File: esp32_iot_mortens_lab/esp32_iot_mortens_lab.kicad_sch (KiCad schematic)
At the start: 55 parts, among them J1 Conn_01x04, J2 Screw_Terminal_01x03, J3 Screw_Terminal_01x08, J4 Screw_Terminal_01x02, J5 USB_C_Receptacle_USB2.0_16P, K1 RT314A05, Q1 UMH3N, Q2 BC817, SW1 SW_SPST, U1 ESP32-WROOM-32D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

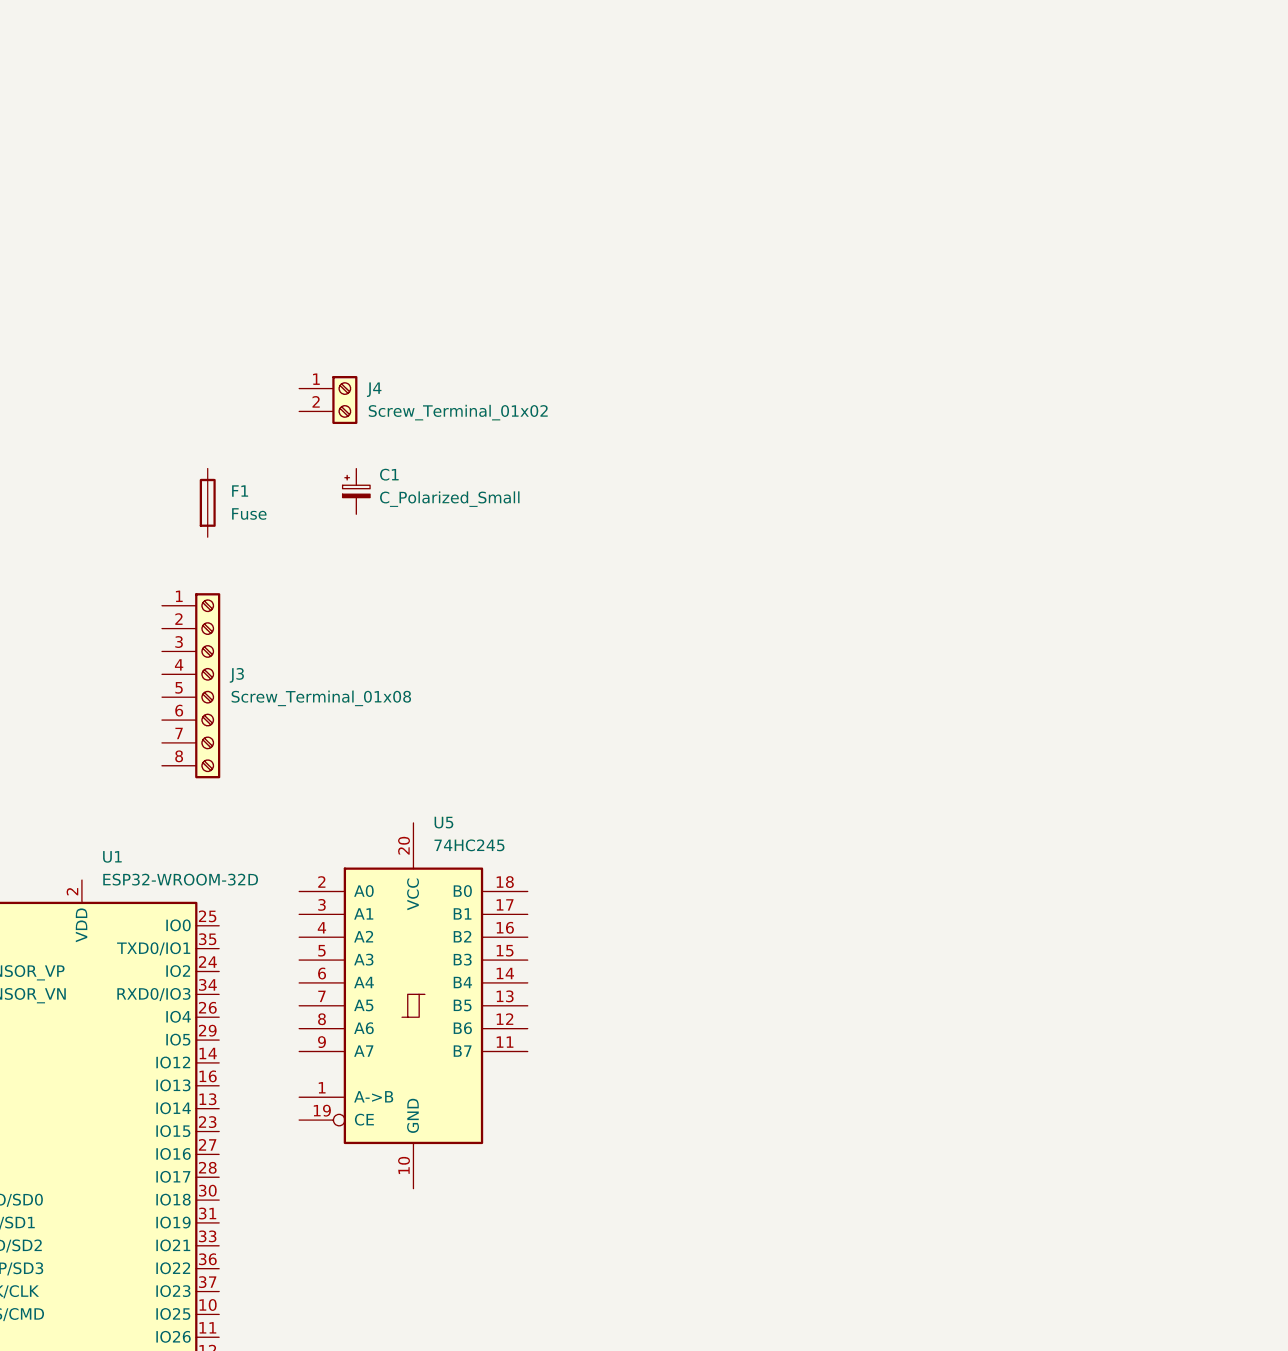
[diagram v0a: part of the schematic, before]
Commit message: bi-directional transceiver subcircuit
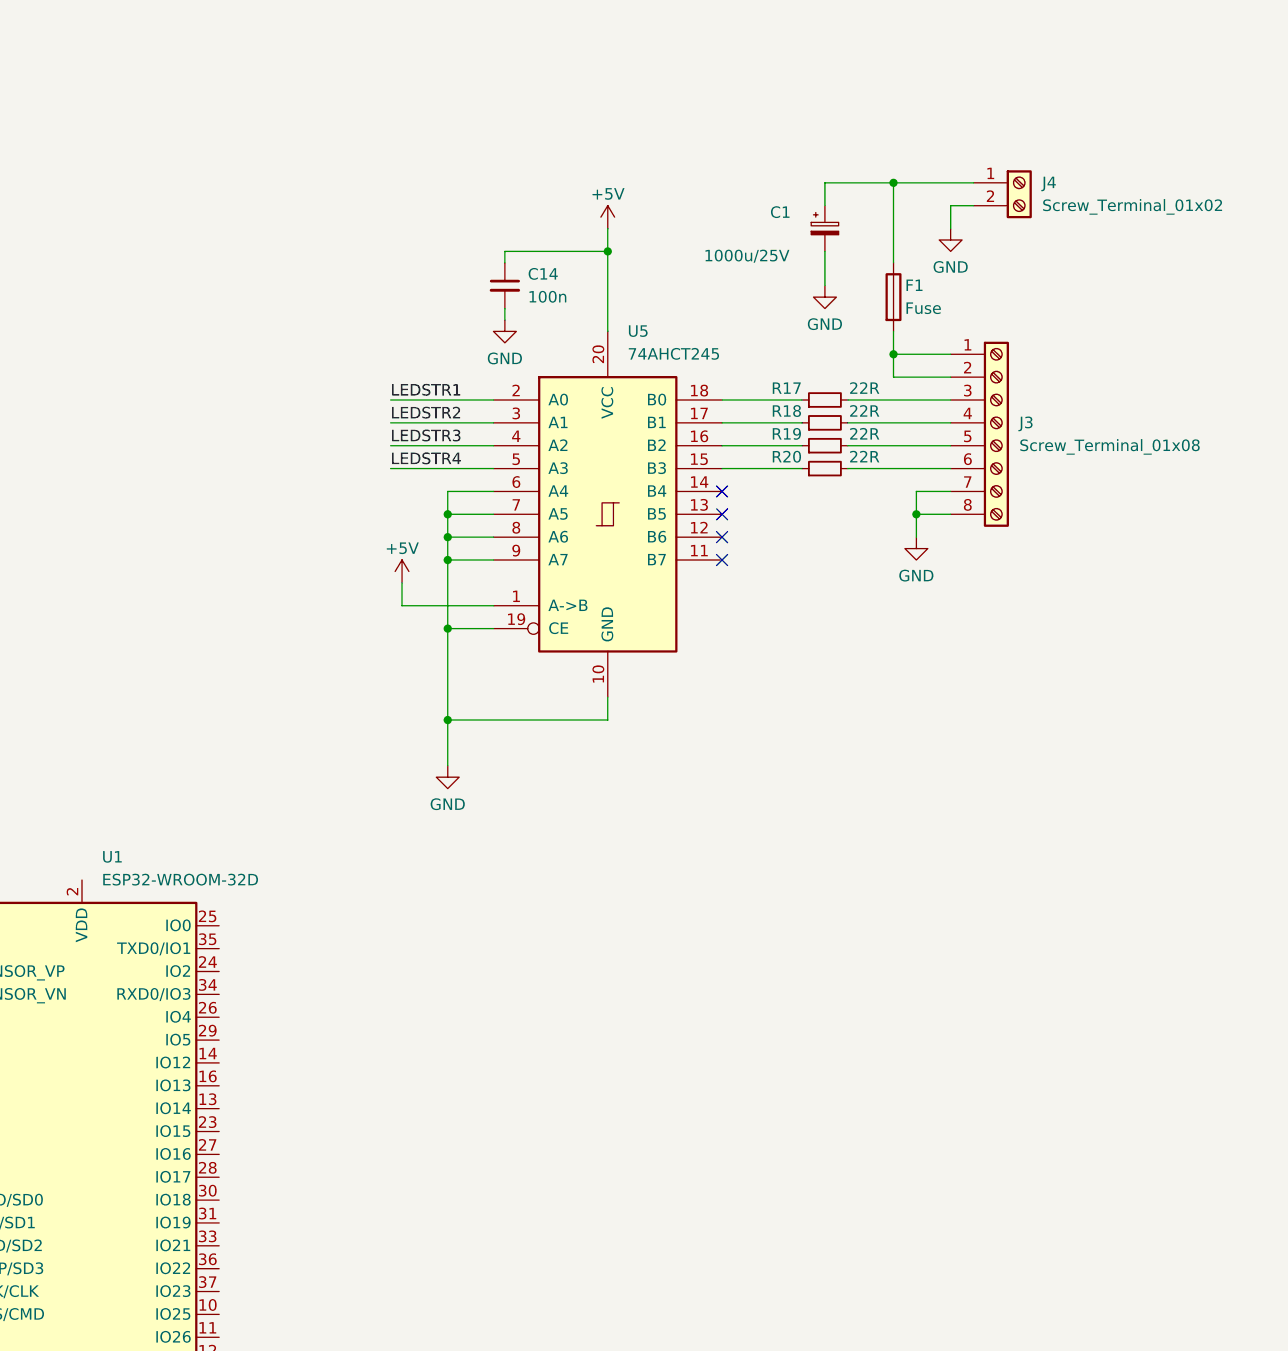
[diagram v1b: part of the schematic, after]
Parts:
- added C14: 100n, symbol Device:C_Small
- added R17, R18, R19, R20: 22R, symbol Device:R_Small
- C1: value C_Polarized_Small -> 1000u/25V
- U5: value 74HC245 -> 74AHCT245
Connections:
- net +3.3VA: now also U5.1 (A->B), U5.20 (VCC), C14.1
- net GND: now also C1.2, J3.7 (Pin_7), J3.8 (Pin_8), J4.2 (Pin_2), U5.10 (GND), U5.19 (CE), U5.6 (A4), U5.7 (A5), U5.8 (A6), U5.9 (A7), C14.2
- net at J4.1 (Pin_1): now also C1.1, F1.1
- net at J3.1 (Pin_1): now also F1.2, J3.2 (Pin_2)
- net at J3.3 (Pin_3): now also R17.2
- net at J3.4 (Pin_4): now also R18.2
- net at J3.5 (Pin_5): now also R19.2
- net at J3.6 (Pin_6): now also R20.2
- net at U5.15 (B3): now also R20.1
- net at U5.16 (B2): now also R19.1
- net at U5.17 (B1): now also R18.1
- net at U5.18 (B0): now also R17.1
- net LEDSTR1: now reaches U5.2 (A0)
- net LEDSTR2: now reaches U5.3 (A1)
- net LEDSTR3: now reaches U5.4 (A2)
- net LEDSTR4: now reaches U5.5 (A3)
- no-connect marks 0 -> 4
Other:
- moved on the sheet: C1, F1, J3, J4, U5

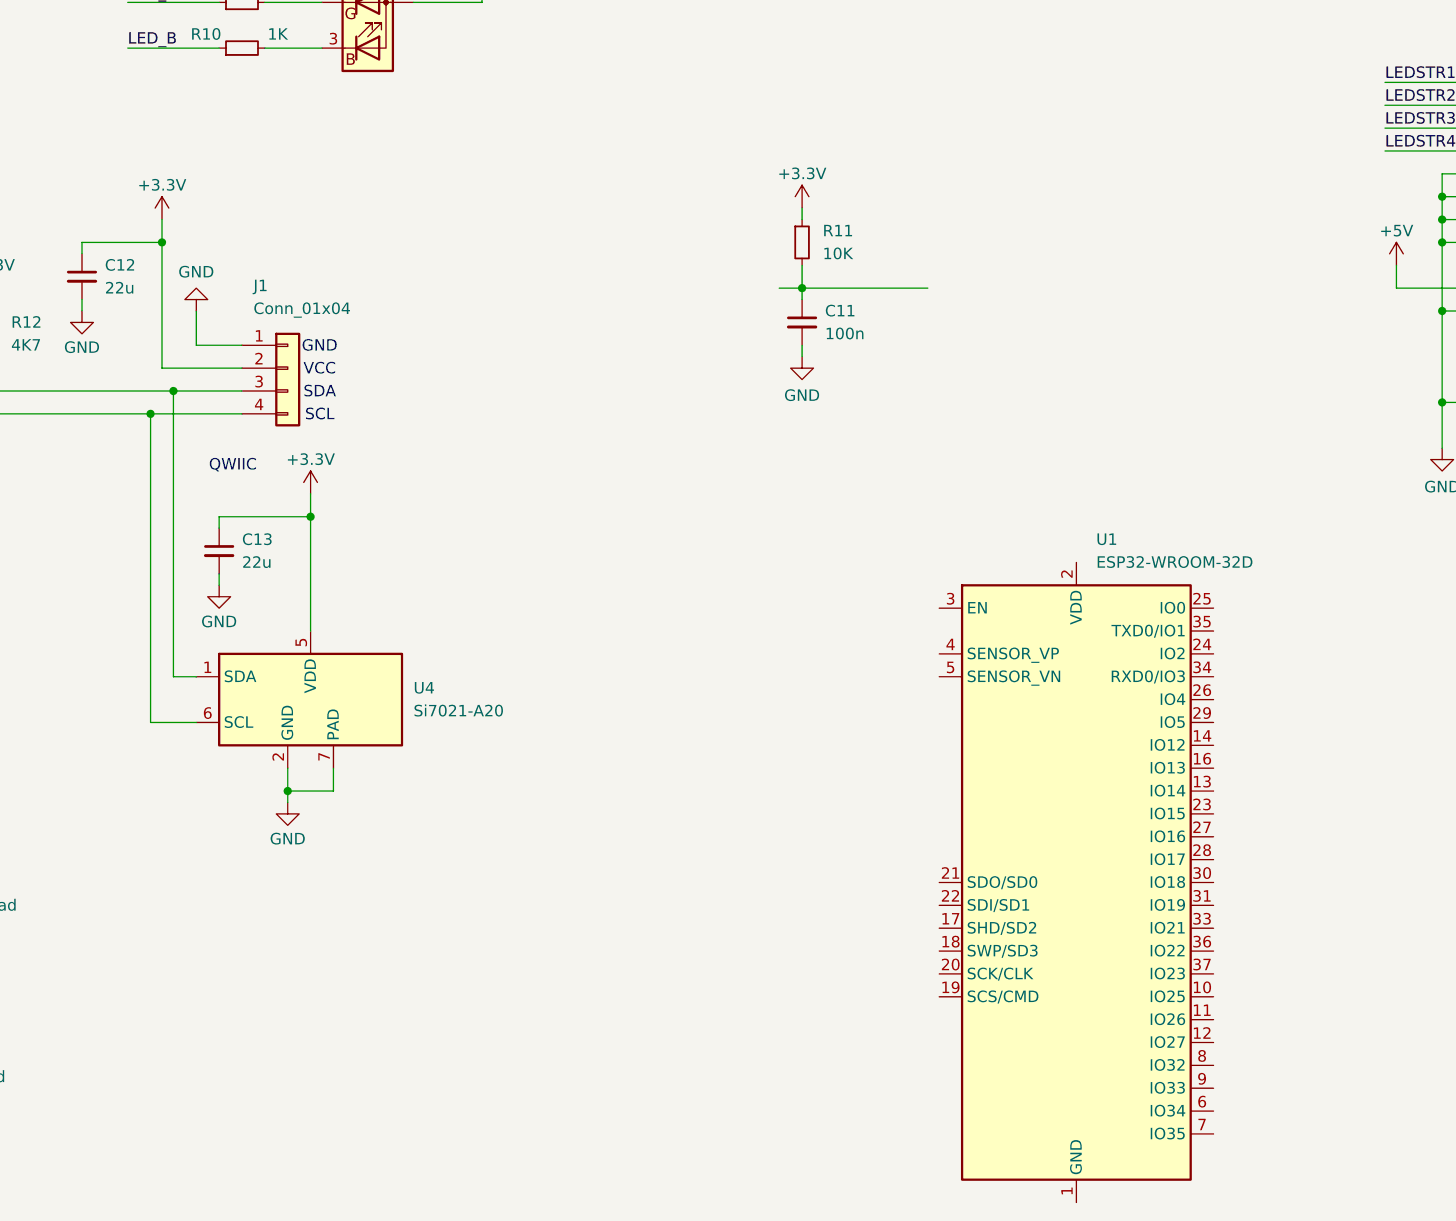
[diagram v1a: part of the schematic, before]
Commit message: starting to connect esp32
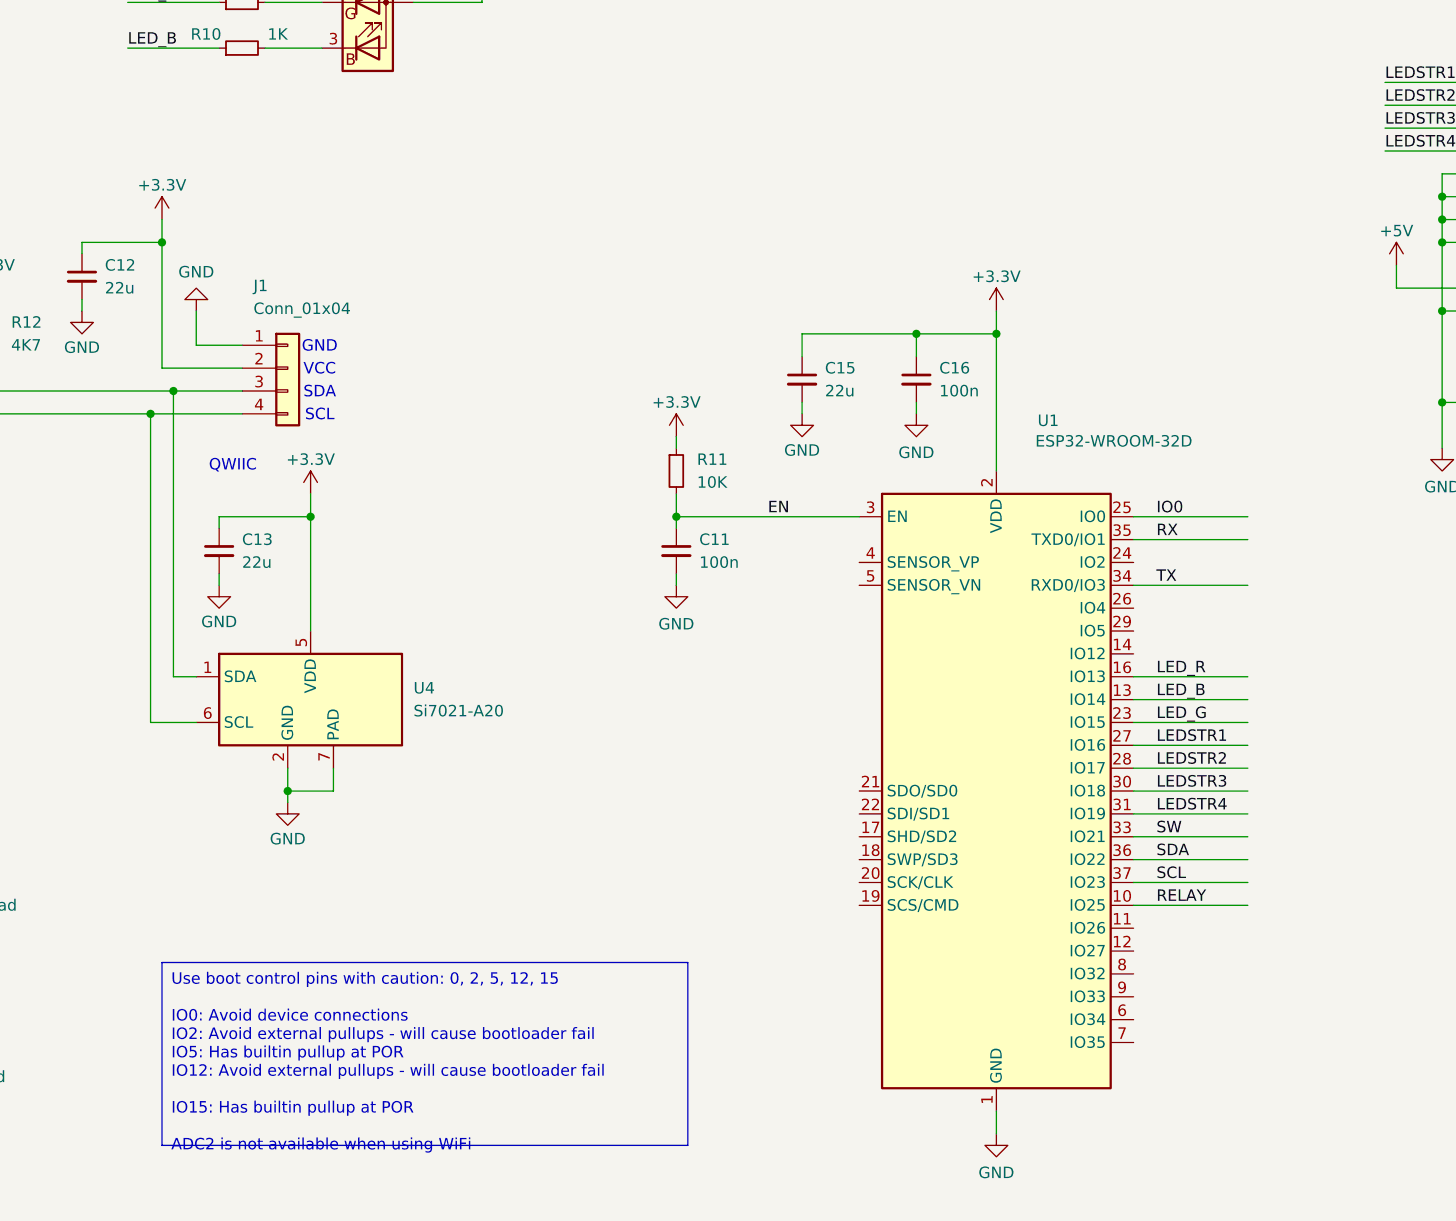
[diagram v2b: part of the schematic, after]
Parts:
- added C15: 22u, symbol Device:C_Small
- added C16: 100n, symbol Device:C_Small
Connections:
- net +3.3V: now also U1.2 (VDD), C15.1, C16.1
- net EN: now also C11.1, R11.2, U1.3 (EN)
- net GND: now also U1.1 (GND), U1.15 (GND), U1.38 (GND), U1.39 (GND), C15.2, C16.2
- net IO0: now also U1.25 (IO0)
- net LEDSTR1: now also U1.27 (IO16)
- net LEDSTR2: now also U1.28 (IO17)
- net LEDSTR3: now also U1.30 (IO18)
- net LEDSTR4: now also U1.31 (IO19)
- net LED_B: now also U1.13 (IO14)
- net LED_G: now also U1.23 (IO15)
- net LED_R: now also U1.16 (IO13)
- net RELAY: now also U1.10 (IO25)
- net RX: now also U1.35 (TXD0/IO1)
- net SCL: now also U1.37 (IO23)
- net SDA: now also U1.36 (IO22)
- net SW: now also U1.33 (IO21)
- net TX: now also U1.34 (RXD0/IO3)
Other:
- moved on the sheet: C11, R11, U1

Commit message: full schematic done
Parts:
- added J6: Conn_02x05_Odd_Even, symbol Connector_Generic:Conn_02x05_Odd_Even
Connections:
- net +3.3V: now also J6.1 (Pin_1), J6.2 (Pin_2)
- net GND: now also J6.10 (Pin_10), J6.9 (Pin_9)
- net GPIO26: now reaches U1.11 (IO26)
- net GPIO26: now also J6.3 (Pin_3)
- net GPIO27: now reaches U1.12 (IO27)
- net GPIO27: now also J6.5 (Pin_5)
- net GPIO34: now reaches U1.6 (IO34)
- net GPIO34: now also J6.6 (Pin_6)
- net GPIO35: now reaches U1.7 (IO35)
- net GPIO35: now also J6.8 (Pin_8)
- net GPIO32: now reaches U1.8 (IO32)
- net GPIO32: now also J6.7 (Pin_7)
- net GPIO33: now reaches U1.9 (IO33)
- net GPIO33: now also J6.4 (Pin_4)
- no-connect marks 4 -> 10
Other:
- note added: "I2C SENSOR + QWIIC CONNECTOR"
- note added: "LDO 5V TO 3.3V"
- note added: "LED DRIVER"
- note added: "MCU"
- note added: "MOUNTING"
- note added: "POWER + PROGRAMMING INTERFACE"
- note added: "RELAY"
- note added: "USER I/O"
- moved on the sheet: C1, C10, C11, C12, C13, C14, C15, C16, C2, C3, C4, C5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
